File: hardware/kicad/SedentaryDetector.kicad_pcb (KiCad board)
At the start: 2 copper layers, 80 x 50 mm, 6 parts, among them J1 ESP32-WROOM-32_2x15, J2 MPU6050_1x8

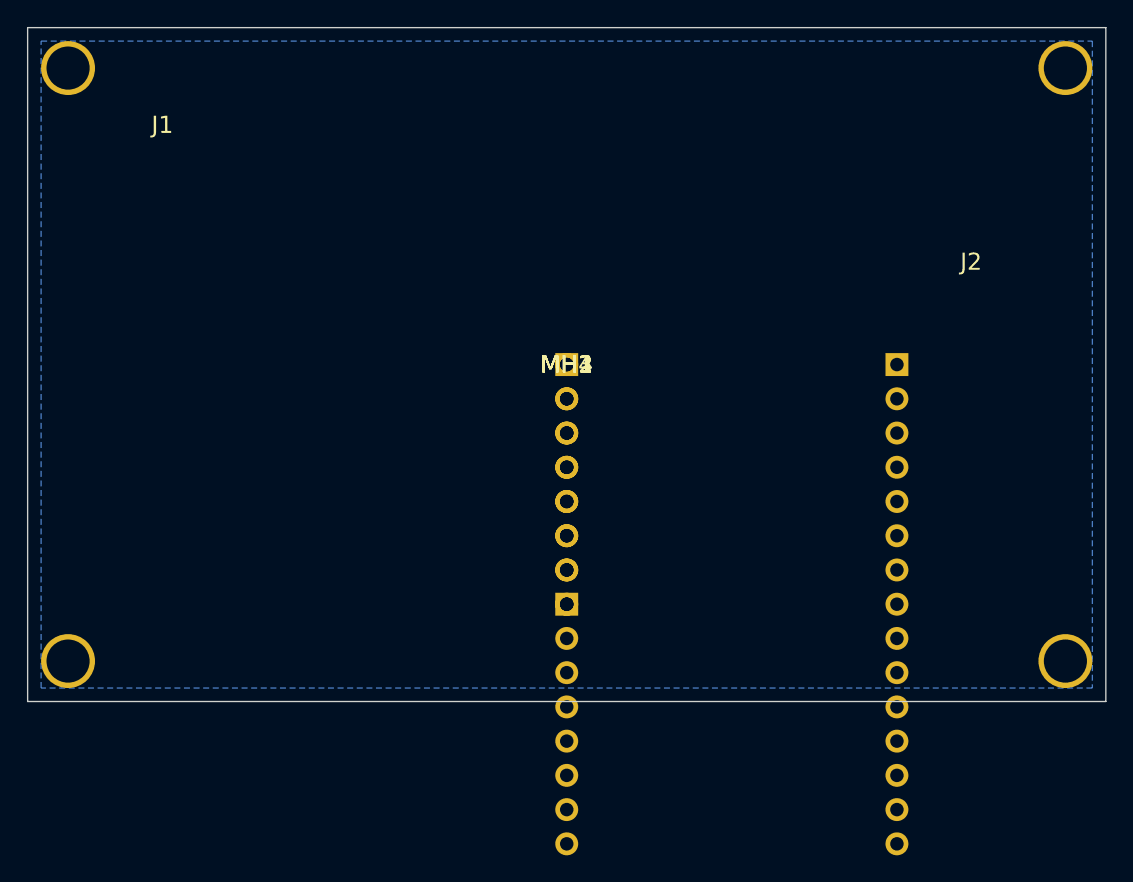
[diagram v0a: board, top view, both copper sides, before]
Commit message: fix(hardware): correct pin spacing to 2.54mm, add I2C/INT routing
PCB fixes:
- Row spacing: 24.5mm -> 2.54mm (standard 0.1in pitch)
- Board: 50x35mm (per AGENTS.md)
- J1: 2x15 @ (-15, -17.8)mm
- J2: 1x8 @ (10, -7.6)mm
- No overlap between connectors

Routing added on F.Cu:
- I2C_SDA: J1.p7 -> J2.p4
- I2C_SCL: J1.p8 -> J2.p3
- 3V3: J1.p2 -> J2.p1
- MPU_INT: J1.p5 -> J2.p8

GND: B.Cu copper pour
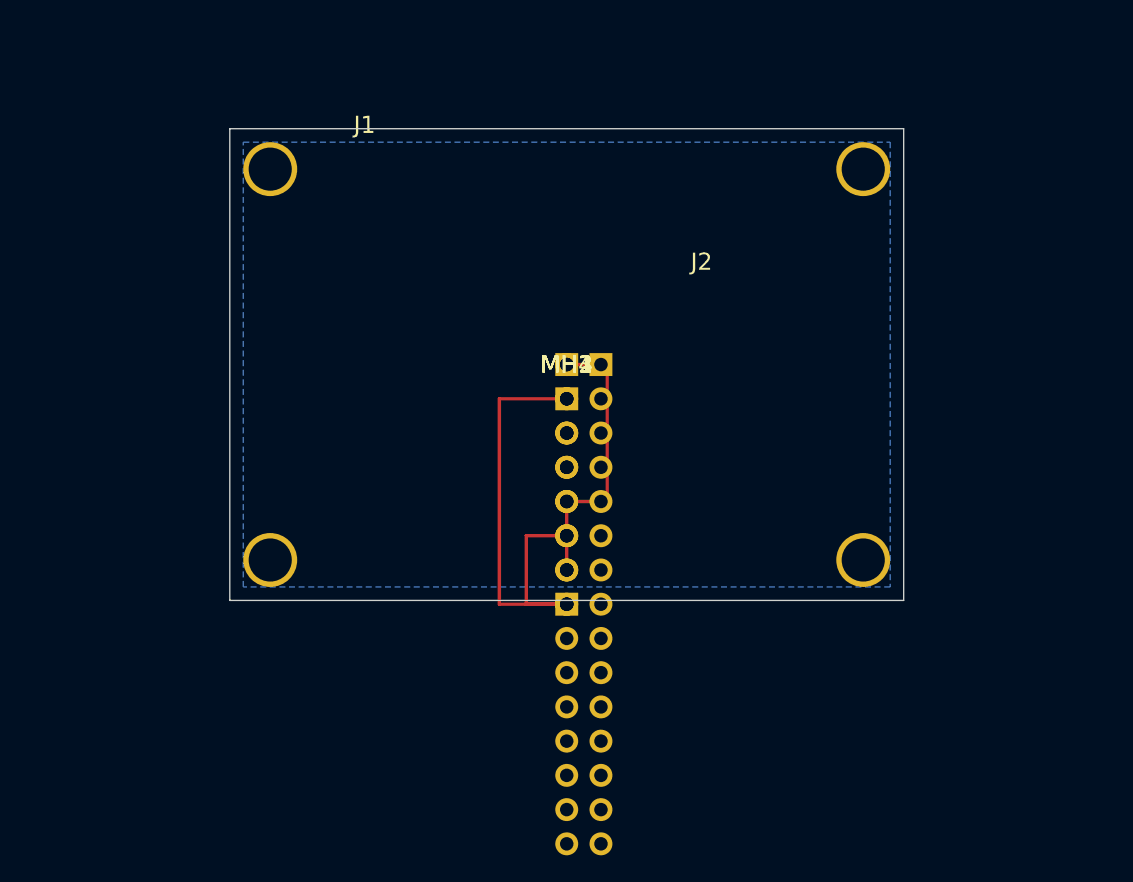
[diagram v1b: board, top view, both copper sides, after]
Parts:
- moved J2 20.0 mm to (10.0, -7.62)
- moved J1 15.0 mm to (-15.0, -17.8)
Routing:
- net 3V3: track 0.00 -> 25.2 mm
- net MPU_INT: track 0.00 -> 16.2 mm
- net I2C_SCL: track 0.00 -> 11.1 mm
- net I2C_SDA: track 0.00 -> 5.08 mm
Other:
- board size 80 x 50 mm -> 50 x 35 mm

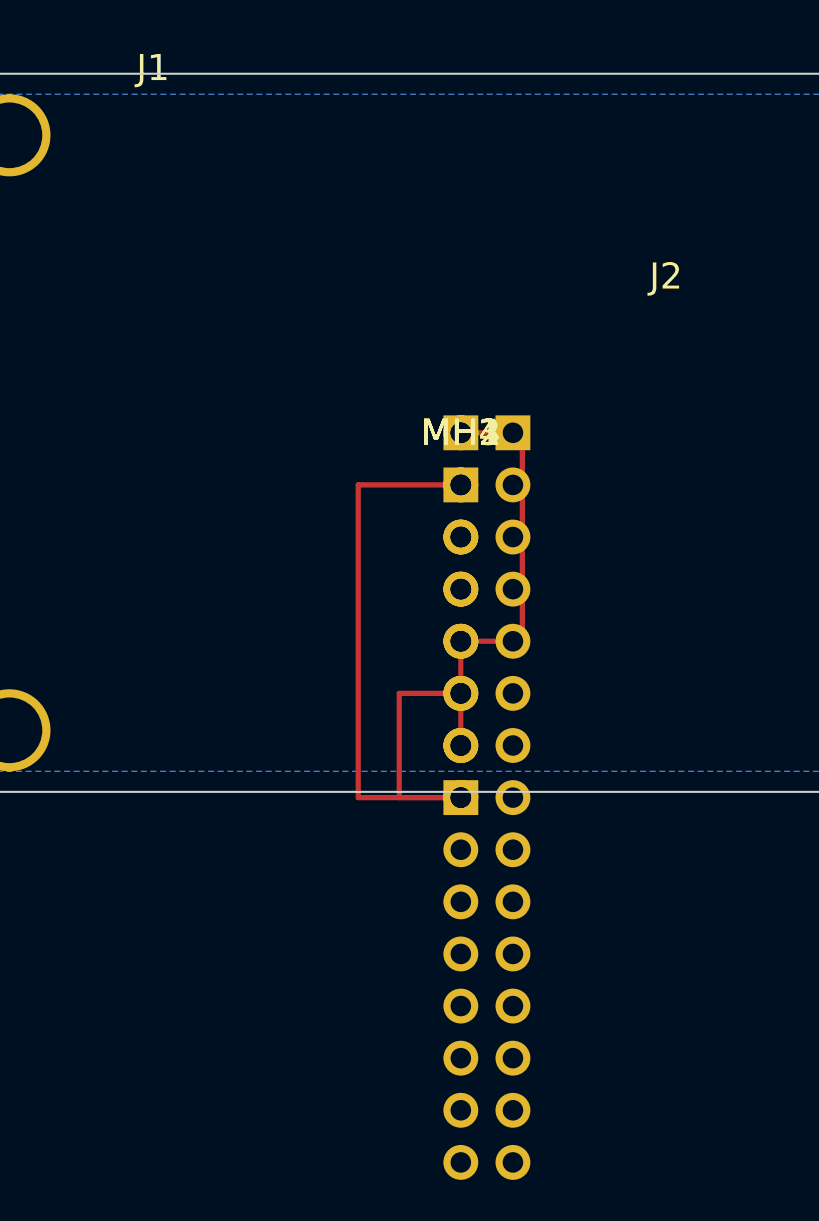
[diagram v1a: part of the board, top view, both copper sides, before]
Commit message: fix(hardware): use absolute pad coordinates, fix connector overlap
- Use absolute pad positions (not relative to footprint)
- J1: x=[-13, -10.5], J2: x=[8] - separated by 18.5mm
- 4 traces: I2C_SDA, I2C_SCL, 3V3, MPU_INT on F.Cu
- GND copper pour on B.Cu
- kicad-happy: 0 errors, PCB passes analysis
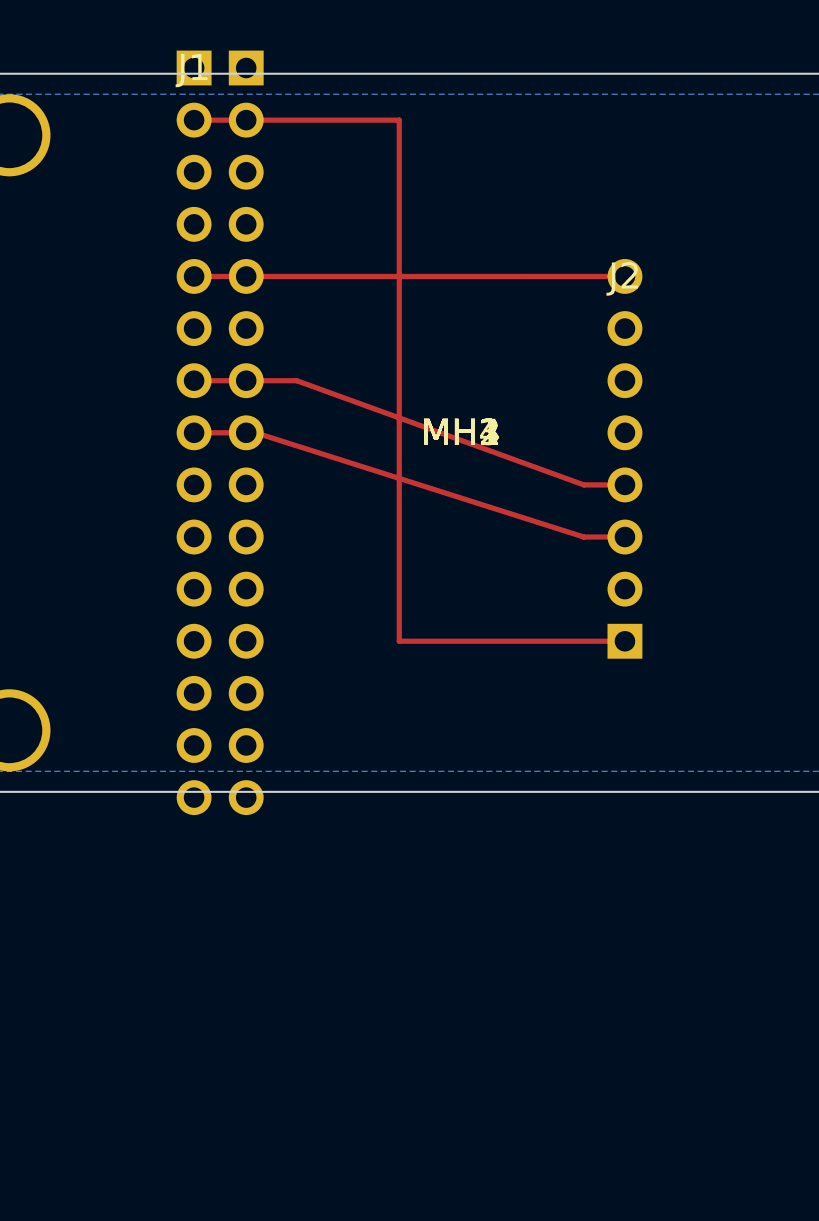
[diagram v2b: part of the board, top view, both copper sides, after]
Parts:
- moved J1 2.00 mm to (-13.0, -17.8)
- moved J2 2.00 mm to (8.00, -7.62)
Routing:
- net 3V3: track 25.2 -> 46.4 mm
- net I2C_SDA: track 5.08 -> 21.9 mm
- net I2C_SCL: track 11.1 -> 21.8 mm
- net MPU_INT: track 16.2 -> 21.0 mm

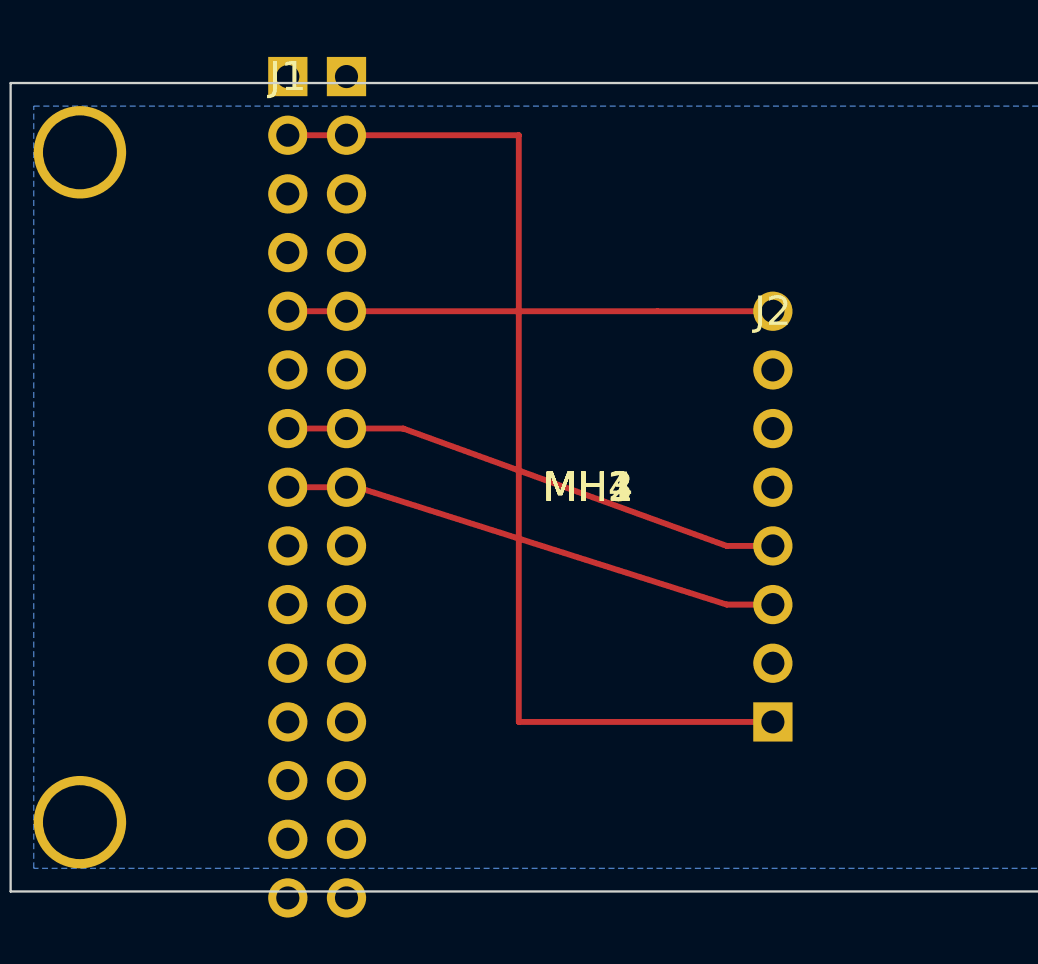
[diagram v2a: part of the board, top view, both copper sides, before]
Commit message: fix(hardware): correct J1 row spacing to 23.5mm
ESP32-WROOM-32 2x15 connector:
- Row spacing: 23.5mm (between left/right columns)
- Pin pitch: 2.54mm (vertical, within each column)
- J1 at x=-18mm (left column), right column at x=-18+23.5=5.5mm

J2 MPU6050 1x8 at x=12mm
Routing: I2C_SDA, I2C_SCL, 3V3, MPU_INT
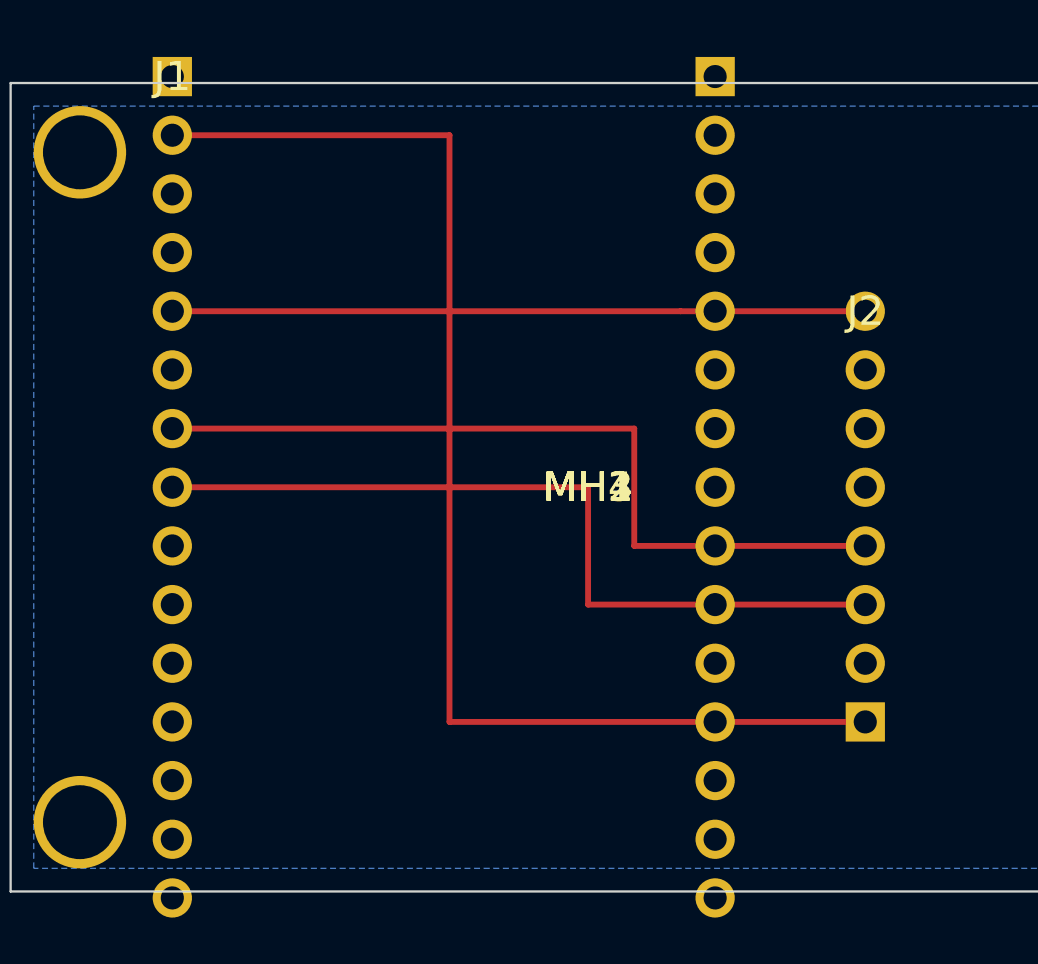
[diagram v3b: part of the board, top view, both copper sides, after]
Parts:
- moved J1 5.00 mm to (-18.0, -17.8)
- moved J2 4.00 mm to (12.0, -7.62)
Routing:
- net I2C_SCL: track 21.8 -> 35.1 mm
- net I2C_SDA: track 21.9 -> 35.1 mm
- net MPU_INT: track 21.0 -> 30.0 mm
- net 3V3: track 46.4 -> 55.4 mm
